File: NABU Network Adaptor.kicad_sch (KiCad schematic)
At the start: 30 parts, among them J2 PC, J3 RF Module, J5 LEDs, U1 SN74LS164N, U10 UA9638CP, U11 UA9637ATC, U12 SN74LS164N, U13 SN74LS164N, U19 LM339N, U20 SN74LS164N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

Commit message: Add appnode path, but I can't make it clickable. :(
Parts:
- U9: AppNote (none) -> Datasheets/TR1863-WesternDigital.pdf
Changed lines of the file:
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@@
+      (effects (font (size 1.27 1.27)) hide)
+    )
+    (property "AppNote" "Datasheets/TR1863-WesternDigital.pdf" (at 451.2547 267.97 0)
       (effects (font (size 1.27 1.27)) hide)
     )

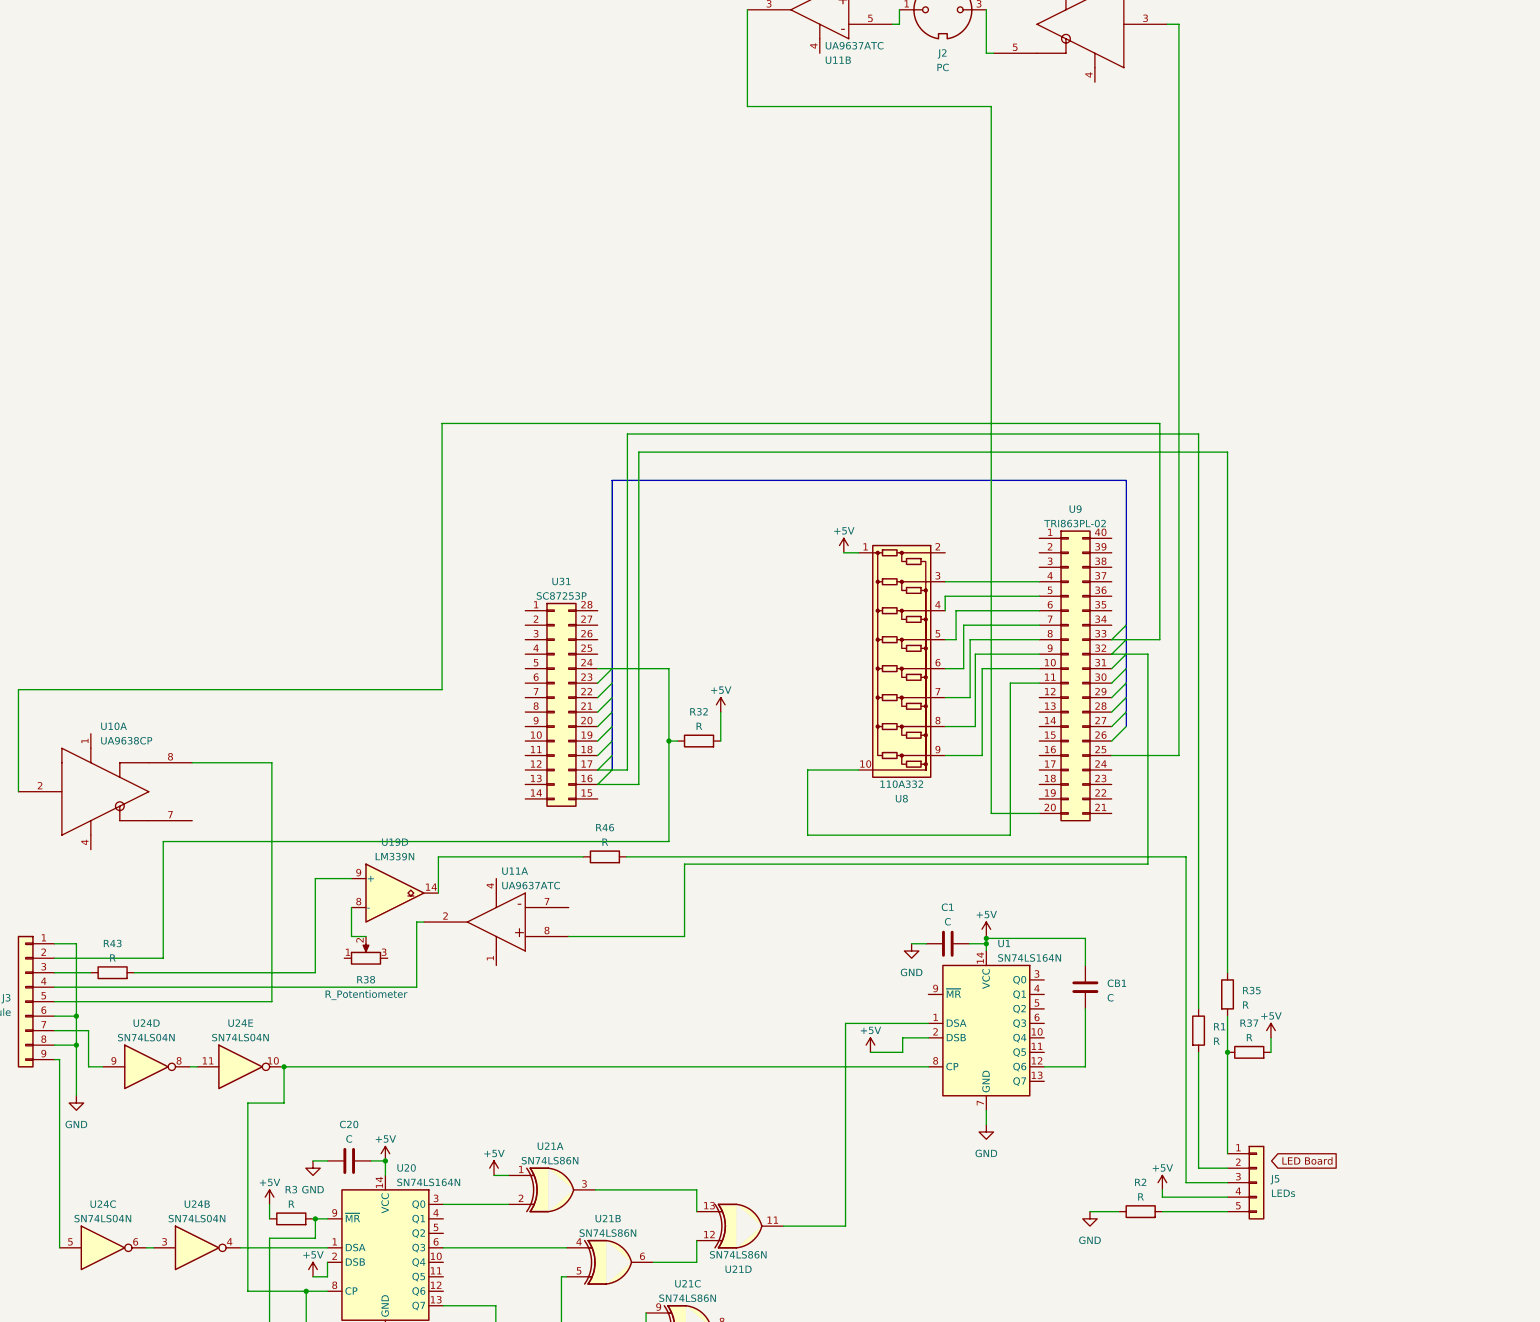
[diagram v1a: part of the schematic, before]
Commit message: Add LED and PSU boards
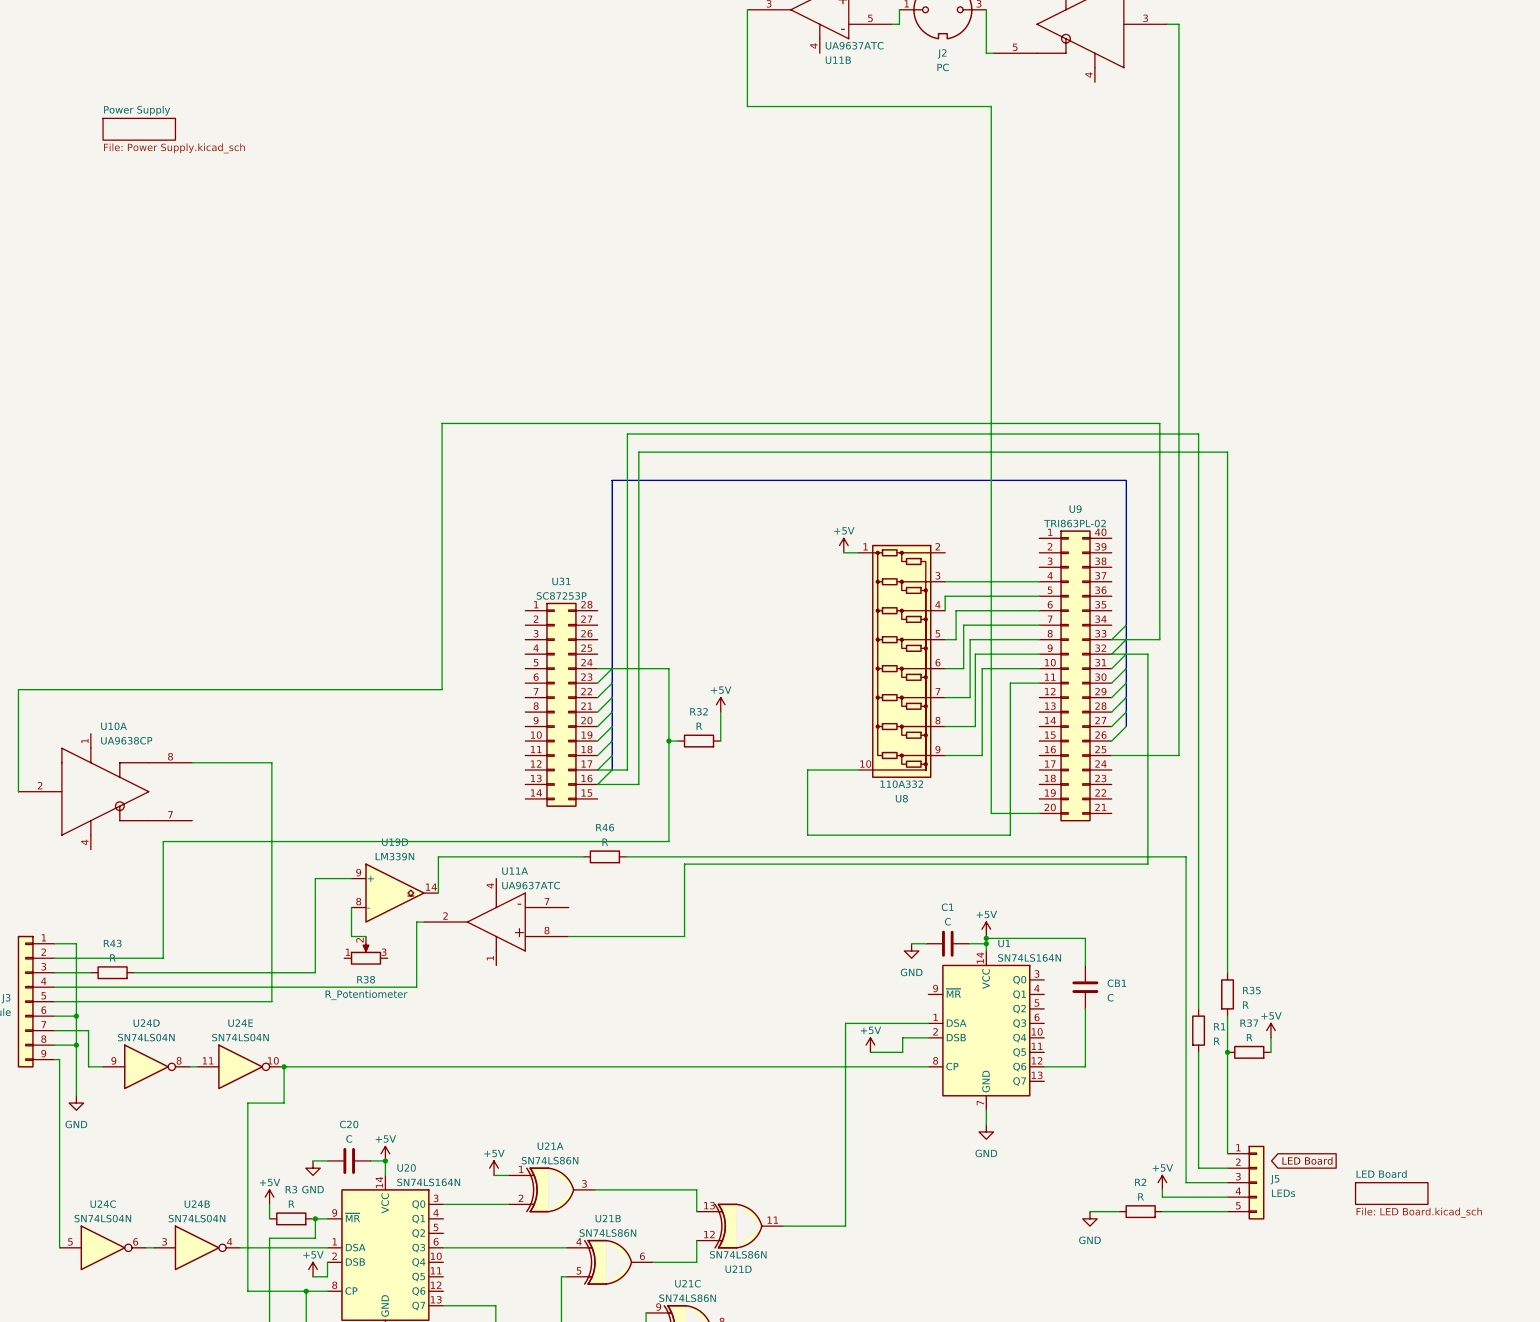
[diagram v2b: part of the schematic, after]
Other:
- added sheet LED Board (LED Board.kicad_sch)
- added sheet Power Supply (Power Supply.kicad_sch)
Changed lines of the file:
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@@
+    )
+  )
+  (sheet (at 501.65 358.14) (size 12.7 3.81) (fields_autoplaced)
+    (stroke (width 0.1524) (type solid))
+    (fill (color 0 0 0 0.0000))
+    (property "Sheetname" "LED Board" (at 501.65 357.4284 0)
+      (effects (font (size 1.27 1.27)) (justify left bottom))
+    )
+    (property "Sheetfile" "LED Board.kicad_sch" (at 501.65 362.5346 0)
+      (effects (font (size 1.27 1.27)) (justify left top))
+    )
+    (instances
+      (project "NABU Network Adaptor"
+        (path "/fe8087f8-6b92-4d5f-81d9-605adde2f076" (page "2"))
+      )
+    )
+  )
+  (sheet (at 281.94 171.45) (size 12.7 3.81) (fields_autoplaced)
+    (stroke (width 0.1524) (type solid))
+    (fill (color 0 0 0 0.0000))
+    (property "Sheetname" "Power Supply" (at 281.94 170.7384 0)
+      (effects (font (size 1.27 1.27)) (justify left bottom))
+    )
+    (property "Sheetfile" "Power Supply.kicad_sch" (at 281.94 175.8446 0)
+      (effects (font (size 1.27 1.27)) (justify left top))
+    )
+    (instances
+      (project "NABU Network Adaptor"
+        (path "/fe8087f8-6b92-4d5f-81d9-605adde2f076" (page "3"))
+      )
     )
   )

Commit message: More of the input from RF deck...
Almost to the FIFO now!
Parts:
- added TP1, TP2: TestPoint, symbol Connector:TestPoint
- added U14: SN74LS04N, symbol 74xx:74LS04
- added U15, U22: SN74LS74AN, symbol 74xx:74LS74
- added U2: 74LS30, symbol 74xx:74LS30
- added unit 7 of U24
- added unit 6 of U24
- added U27: SN74LS00P, symbol 74xx:74LS00
- added U3: 74LS27, symbol 74xx:74LS27
- added U4: SN74LS164N, symbol 74xx:74HCT164
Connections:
- net +5V: now also U4.2 (DSB)
- net GND: now also U3.1, U3.3, U3.7 (GND)
- net at R3.2, U12.9 (~{MR}), U13.9 (~{MR})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: now also U1.9 (~{MR}), U22.4 (~{S}), U4.9 (~{MR})
- net at U1.8 (CP), U12.8 (CP), U13.8 (CP)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: now also U14.3
- net at U1.10 (Q4): now also U2.5
- net at U1.11 (Q5): now also U2.4
- net at U1.13 (Q7): now also U3.9
- net at U1.3 (Q0): now also TP1.1, U14.1, U4.1 (DSA)
- net at U1.4 (Q1): now also U2.1
- net at U1.5 (Q2): now also U2.2
- net at U1.6 (Q3): now also U2.3
- new net: U14.12, U3.10
- new net: U2.8, U3.11, U3.5
- new net: U14.11, U3.8
- new net: U14.10, U15.10 (~{S}), U15.4 (~{S})
- new net: U14.13, U3.4
- new net: U14.4, U14.5
- new net: U14.6, U3.13
- new net: TP2.1, U24.13, U3.12, U4.8 (CP)
- new net: U3.2, U3.6
- new net: U14.2, U2.6
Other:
- moved on the sheet: CB1, J5, R1, R2, R35, R37, U21E
